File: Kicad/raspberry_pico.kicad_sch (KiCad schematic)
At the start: 5 parts, among them Q1201 DMG2305UX, U1201 Pico

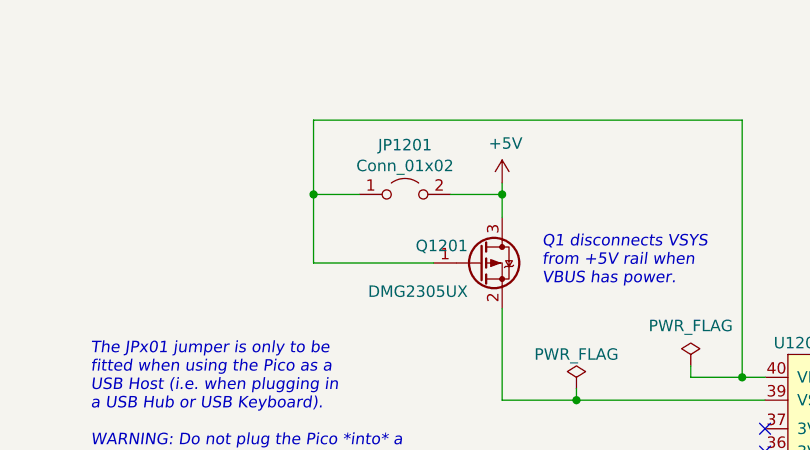
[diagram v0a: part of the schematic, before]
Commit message: Cleaned up the part numbers.
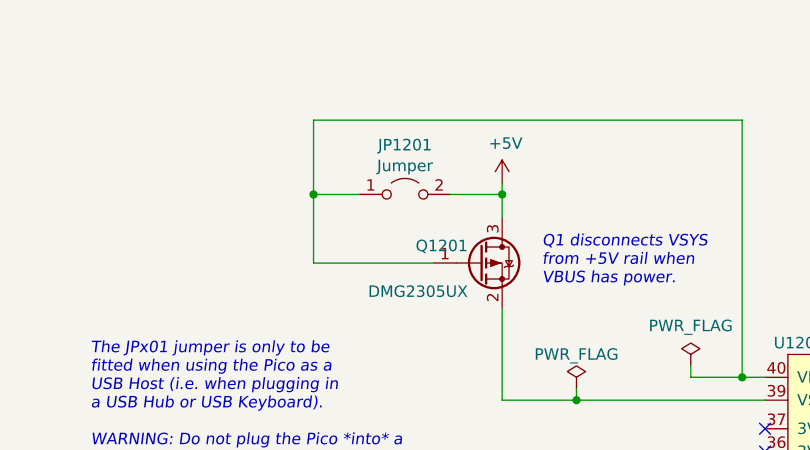
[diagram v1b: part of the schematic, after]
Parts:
- JP1201: value Conn_01x02 -> Jumper
- Q1201: Digikey DMG2305UX-13DICT-ND -> (none); JLCPCB Collection (none) -> Extended
- R1201, R1202: Digikey RMCF0805FT2K00CT-ND -> (none); JLCPCB Collection (none) -> Basic; MPN RMCF0805FT2K00 -> 0805W8F2001T5E; Manufacturer Stackpole -> Uniroyal
- U1201: MPN SC0915 -> Pico
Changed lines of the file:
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@@
       (effects (font (size 1.27 1.27)) hide)
     )
-    (property "MPN" "SC0915" (id 6) (at 132.08 50.8 0)
+    (property "MPN" "Pico" (id 6) (at 132.08 50.8 0)
       (effects (font (size 1.27 1.27)) hide)
     )
@@
     )
     (property "Voltage" "~" (id 11) (at 132.08 50.8 0)
+      (effects (font (size 1.27 1.27)) hide)
+    )
+    (property "JLCPCB Collection" "~" (id 12) (at 132.08 50.8 0)
       (effects (font (size 1.27 1.27)) hide)
     )
@@
       (effects (font (size 1.27 1.27)) hide)
     )
-    (property "Digikey" "RMCF0805FT2K00CT-ND" (id 5) (at 212.725 84.455 0)
-      (effects (font (size 1.27 1.27)) hide)
-    )
-    (property "MPN" "RMCF0805FT2K00" (id 6) (at 212.725 84.455 0)
-      (effects (font (size 1.27 1.27)) hide)
-    )
-    (property "Manufacturer" "Stackpole" (id 7) (at 212.725 84.455 0)
+    (property "Digikey" "~" (id 5) (at 212.725 84.455 0)
+      (effects (font (size 1.27 1.27)) hide)
+    )
+    (property "MPN" "0805W8F2001T5E" (id 6) (at 212.725 84.455 0)
+      (effects (font (size 1.27 1.27)) hide)
+    )
+    (property "Manufacturer" "Uniroyal" (id 7) (at 212.725 84.455 0)
       (effects (font (size 1.27 1.27)) hide)
     )
@@
     )
     (property "Mouser" "~" (id 11) (at 212.725 84.455 0)
+      (effects (font (size 1.27 1.27)) hide)
+    )
+    (property "JLCPCB Collection" "Basic" (id 12) (at 212.725 84.455 0)
       (effects (font (size 1.27 1.27)) hide)
     )
@@
       (effects (font (size 1.27 1.27)) hide)
     )
-    (property "Digikey" "RMCF0805FT2K00CT-ND" (id 5) (at 202.565 84.455 0)
-      (effects (font (size 1.27 1.27)) hide)
-    )
-    (property "MPN" "RMCF0805FT2K00" (id 6) (at 202.565 84.455 0)
-      (effects (font (size 1.27 1.27)) hide)
-    )
-    (property "Manufacturer" "Stackpole" (id 7) (at 202.565 84.455 0)
+    (property "Digikey" "~" (id 5) (at 202.565 84.455 0)
+      (effects (font (size 1.27 1.27)) hide)
+    )
+    (property "MPN" "0805W8F2001T5E" (id 6) (at 202.565 84.455 0)
+      (effects (font (size 1.27 1.27)) hide)
+    )
+    (property "Manufacturer" "Uniroyal" (id 7) (at 202.565 84.455 0)
       (effects (font (size 1.27 1.27)) hide)
     )
@@
       (effects (font (size 1.27 1.27)) hide)
     )
+    (property "JLCPCB Collection" "Basic" (id 12) (at 202.565 84.455 0)
+      (effects (font (size 1.27 1.27)) hide)
+    )
     (pin "1")
     (pin "2")
@@
     (in_bom yes) (on_board yes)
     (property "Reference" "JP1201" (id 0) (at 89.535 27.5336 0))
-    (property "Value" "Conn_01x02" (id 1) (at 89.535 29.845 0))
+    (property "Value" "Jumper" (id 1) (at 89.535 29.845 0))
     (property "Footprint" "Connector_PinHeader_2.54mm:PinHeader_1x02_P2.54mm_Vertical" (id 2) (at 89.535 33.02 0)
       (effects (font (size 1.27 1.27)) hide)
@@
       (effects (font (size 1.27 1.27)) hide)
     )
+    (property "JLCPCB Collection" "~" (id 12) (at 89.535 33.02 0)
+      (effects (font (size 1.27 1.27)) hide)
+    )
     (pin "1")
     (pin "2")
@@
       (effects (font (size 1.27 1.27)) hide)
     )
-    (property "Datasheet" "https://www.diodes.com/assets/Datasheets/DMG2305UX.pdf" (id 3) (at 97.79 40.64 0)
+    (property "Datasheet" "" (id 3) (at 97.79 40.64 0)
       (effects (font (size 1.27 1.27)) hide)
     )
@@
       (effects (font (size 1.27 1.27)) hide)
     )
-    (property "Digikey" "DMG2305UX-13DICT-ND" (id 5) (at 97.79 40.64 0)
+    (property "Digikey" "~" (id 5) (at 97.79 40.64 0)
       (effects (font (size 1.27 1.27)) hide)
     )
@@
       (effects (font (size 1.27 1.27)) hide)
     )
+    (property "JLCPCB Collection" "Extended" (id 12) (at 97.79 40.64 0)
+      (effects (font (size 1.27 1.27)) hide)
+    )

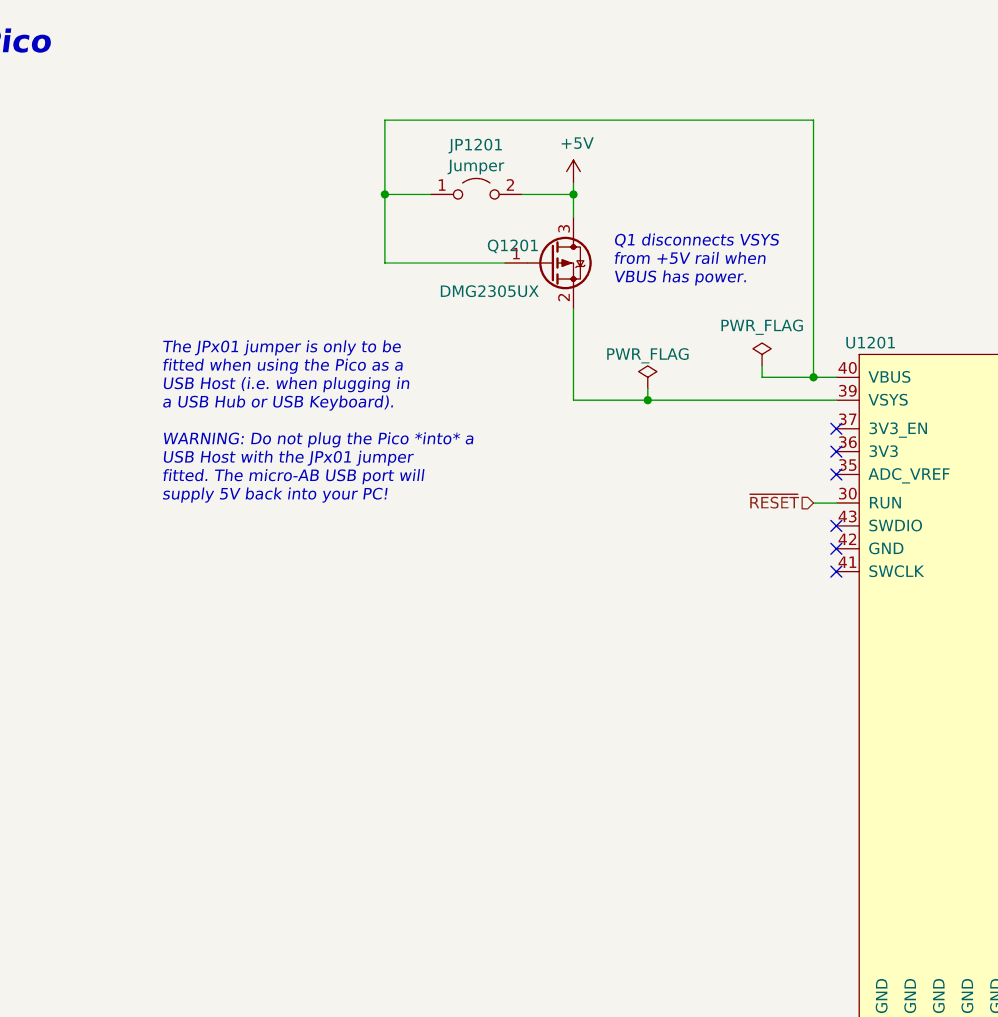
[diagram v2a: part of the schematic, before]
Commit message: Replaced decoupling caps, and worked on PCB layout.
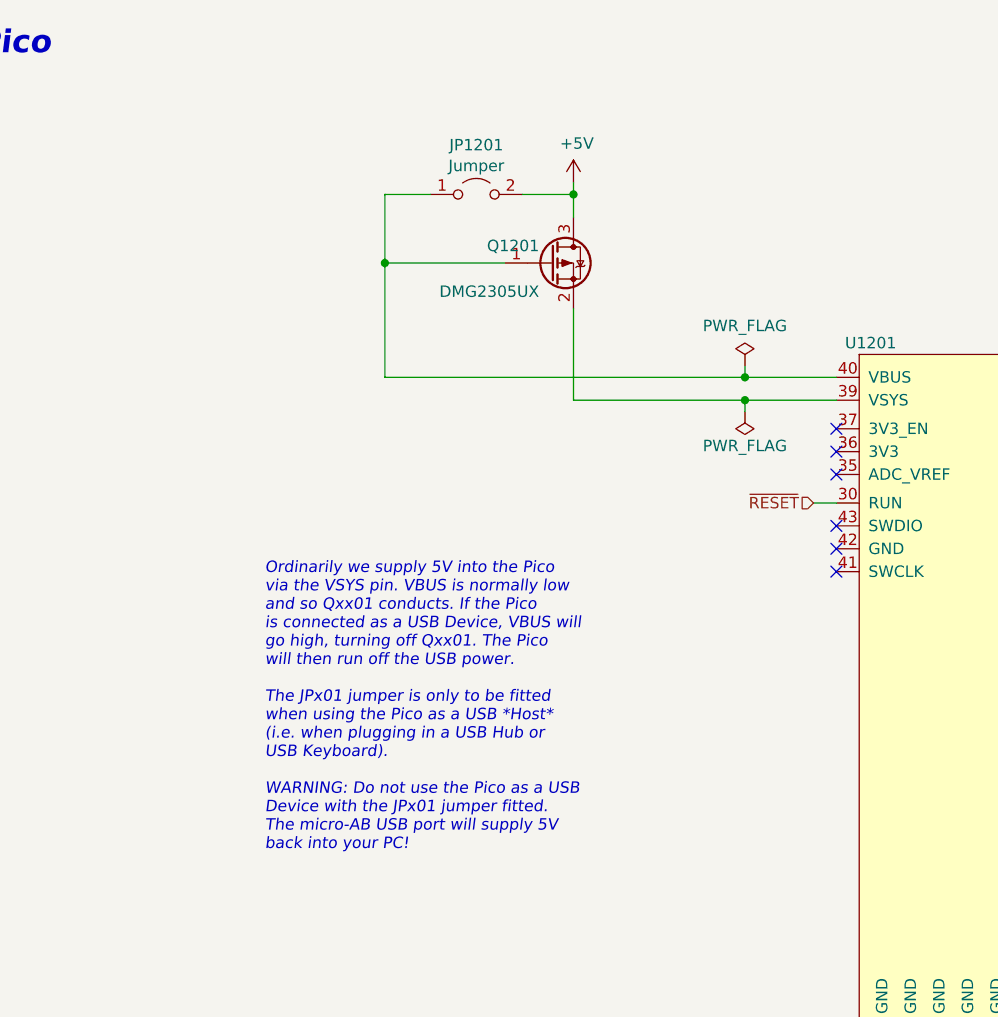
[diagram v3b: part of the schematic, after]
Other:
- note added: "Ordinarily we supply 5V into the Pico via the VSYS pin. VBUS is normally low and so Qxx01 conducts. If the Pico is connected as a USB Device, VBUS will go high, turning off Qxx01. The Pico will then run off the USB power. The JPx01 jumper is only to be fitted when using the Pico as a USB *Host* (i.e. when plugging in a USB Hub or USB Keyboard). WARNING: Do not use the Pico as a USB Device with th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"
- note removed: "Q1 disconnects VSYS from +5V rail when VBUS has power."
- note removed: "The JPx01 jumper is only to be fitted when using the Pico as a USB Host (i.e. when plugging in a USB Hub or USB Keyboard). WARNING: Do not plug the Pico *into* a USB Host with the JPx01 jumper fitted. The micro-AB USB port will supply 5V back into your PC!"
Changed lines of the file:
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@@
     (comment 2 "Copyright (c) The Neotron Developers, 2022")
   )
-  (junction (at 79.375 33.02) (diameter 0) (color 0 0 0 0)
-  )
   (junction (at 150.495 128.27) (diameter 0) (color 0 0 0 0)
   )
   (junction (at 137.795 128.27) (diameter 0) (color 0 0 0 0)
   )
-  (junction (at 108.585 55.88) (diameter 0) (color 0 0 0 0)
+  (junction (at 119.38 55.88) (diameter 0) (color 0 0 0 0)
+  )
+  (junction (at 119.38 53.34) (diameter 0) (color 0 0 0 0)
   )
   (junction (at 144.145 128.27) (diameter 0) (color 0 0 0 0)
@@
   (junction (at 140.97 128.27) (diameter 0) (color 0 0 0 0)
   )
+  (junction (at 79.375 40.64) (diameter 0) (color 0 0 0 0)
+  )
   (junction (at 212.725 79.375) (diameter 0) (color 0 0 0 0)
-  )
-  (junction (at 127 53.34) (diameter 0) (color 0 0 0 0)
   )
   (no_connect (at 129.54 72.39))
@@
     (stroke (width 0) (type default) (color 0 0 0 0))
   )
-  (wire (pts (xy 79.375 24.765) (xy 127 24.765))
+  (wire (pts (xy 79.375 53.34) (xy 119.38 53.34))
     (stroke (width 0) (type default) (color 0 0 0 0))
   )
@@
     (stroke (width 0) (type default) (color 0 0 0 0))
   )
-  (wire (pts (xy 127 24.765) (xy 127 53.34))
-    (stroke (width 0) (type default) (color 0 0 0 0))
-  )
   (wire (pts (xy 165.1 53.34) (xy 167.64 53.34))
     (stroke (width 0) (type default) (color 0 0 0 0))
   )
-  (wire (pts (xy 108.585 54.61) (xy 108.585 55.88))
+  (wire (pts (xy 119.38 57.15) (xy 119.38 55.88))
     (stroke (width 0) (type default) (color 0 0 0 0))
   )
@@
     (stroke (width 0) (type default) (color 0 0 0 0))
   )
+  (wire (pts (xy 119.38 53.34) (xy 129.54 53.34))
+    (stroke (width 0) (type default) (color 0 0 0 0))
+  )
   (wire (pts (xy 212.725 91.44) (xy 212.725 88.265))
     (stroke (width 0) (type default) (color 0 0 0 0))
@@
     (stroke (width 0) (type default) (color 0 0 0 0))
   )
-  (wire (pts (xy 121.285 53.34) (xy 127 53.34))
-    (stroke (width 0) (type default) (color 0 0 0 0))
-  )
   (wire (pts (xy 137.795 128.27) (xy 137.795 127.635))
     (stroke (width 0) (type default) (color 0 0 0 0))
@@
     (stroke (width 0) (type default) (color 0 0 0 0))
   )
-  (wire (pts (xy 127 53.34) (xy 129.54 53.34))
-    (stroke (width 0) (type default) (color 0 0 0 0))
-  )
   (wire (pts (xy 94.615 33.02) (xy 100.33 33.02))
     (stroke (width 0) (type default) (color 0 0 0 0))
@@
     (stroke (width 0) (type default) (color 0 0 0 0))
   )
-  (wire (pts (xy 108.585 55.88) (xy 129.54 55.88))
+  (wire (pts (xy 119.38 55.88) (xy 129.54 55.88))
     (stroke (width 0) (type default) (color 0 0 0 0))
   )
@@
     (stroke (width 0) (type default) (color 0 0 0 0))
   )
-  (wire (pts (xy 100.33 55.88) (xy 108.585 55.88))
+  (wire (pts (xy 100.33 55.88) (xy 119.38 55.88))
     (stroke (width 0) (type default) (color 0 0 0 0))
   )
@@
     (stroke (width 0) (type default) (color 0 0 0 0))
   )
-  (wire (pts (xy 79.375 24.765) (xy 79.375 33.02))
+  (wire (pts (xy 79.375 53.34) (xy 79.375 40.64))
     (stroke (width 0) (type default) (color 0 0 0 0))
   )
@@
     (stroke (width 0) (type default) (color 0 0 0 0))
   )
-  (wire (pts (xy 121.285 52.07) (xy 121.285 53.34))
+  (wire (pts (xy 119.38 52.07) (xy 119.38 53.34))
     (stroke (width 0) (type default) (color 0 0 0 0))
   )
@@
     (stroke (width 0) (type default) (color 0 0 0 0))
   )
-  (text "Q1 disconnects VSYS\nfrom +5V rail when\nVBUS has power."
-    (at 104.775 43.18 0)
-    (effects (font (size 1.27 1.27) italic) (justify left bottom))
-  )
-  (text "The JPx01 jumper is only to be\nfitted when using the Pico as a\nUSB Host (i.e. when plugging in\na USB Hub or USB Keyboard).\n\nWARNING: Do not plug the Pico *into* a\nUSB Host with the JPx01 jumper\nfitted. The micro-AB USB port will\nsupply 5V back into your PC!"
-    (at 54.61 67.31 0)
+  (text "Ordinarily we supply 5V into the Pico\nvia the VSYS pin. VBUS is normally low\nand so Qxx01 conducts. If the Pico\nis connected as a USB Device, VBUS will\ngo high, turning off Qxx01. The Pico\nwill then run off the USB power.\n\nThe JPx01 jumper is only to be fitted\nwhen using the Pico as a USB *Host*\n(i.e. when plugging in a USB Hub or\nUSB Keyboard).\n\nWARNING: Do not use the Pico as a USB\nDevice with the JPx01 jumper fitted.\nThe micro-AB USB port will supply 5V\nback into your PC!"
+    (at 66.04 106.045 0)
     (effects (font (size 1.27 1.27) italic) (justify left bottom))
   )
@@
     (pin "9")
   )
-  (symbol (lib_id "power:PWR_FLAG") (at 121.285 52.07 0) (mirror y) (unit 1)
-    (in_bom yes) (on_board yes)
-    (property "Reference" "#FLG01201" (id 0) (at 121.285 50.165 0)
-      (effects (font (size 1.27 1.27)) hide)
-    )
-    (property "Value" "PWR_FLAG" (id 1) (at 121.285 47.625 0))
-    (property "Footprint" "" (id 2) (at 121.285 52.07 0)
-      (effects (font (size 1.27 1.27)) hide)
-    )
-    (property "Datasheet" "~" (id 3) (at 121.285 52.07 0)
+  (symbol (lib_id "power:PWR_FLAG") (at 119.38 52.07 0) (mirror y) (unit 1)
+    (in_bom yes) (on_board yes)
+    (property "Reference" "#FLG01201" (id 0) (at 119.38 50.165 0)
+      (effects (font (size 1.27 1.27)) hide)
+    )
+    (property "Value" "PWR_FLAG" (id 1) (at 119.38 47.625 0))
+    (property "Footprint" "" (id 2) (at 119.38 52.07 0)
+      (effects (font (size 1.27 1.27)) hide)
+    )
+    (property "Datasheet" "~" (id 3) (at 119.38 52.07 0)
       (effects (font (size 1.27 1.27)) hide)
     )
@@
     (pin "1")
   )
-  (symbol (lib_id "power:PWR_FLAG") (at 108.585 54.61 0) (mirror y) (unit 1)
-    (in_bom yes) (on_board yes)
-    (property "Reference" "#FLG01202" (id 0) (at 108.585 52.705 0)
-      (effects (font (size 1.27 1.27)) hide)
-    )
-    (property "Value" "PWR_FLAG" (id 1) (at 108.585 50.8 0))
-    (property "Footprint" "" (id 2) (at 108.585 54.61 0)
-      (effects (font (size 1.27 1.27)) hide)
-    )
-    (property "Datasheet" "~" (id 3) (at 108.585 54.61 0)
+  (symbol (lib_id "power:PWR_FLAG") (at 119.38 57.15 0) (mirror x) (unit 1)
+    (in_bom yes) (on_board yes)
+    (property "Reference" "#FLG01202" (id 0) (at 119.38 59.055 0)
+      (effects (font (size 1.27 1.27)) hide)
+    )
+    (property "Value" "PWR_FLAG" (id 1) (at 119.38 60.96 0))
+    (property "Footprint" "" (id 2) (at 119.38 57.15 0)
+      (effects (font (size 1.27 1.27)) hide)
+    )
+    (property "Datasheet" "~" (id 3) (at 119.38 57.15 0)
       (effects (font (size 1.27 1.27)) hide)
     )
@@
       (effects (font (size 1.27 1.27)) hide)
     )
-    (property "Datasheet" "" (id 3) (at 97.79 40.64 0)
-      (effects (font (size 1.27 1.27)) hide)
-    )
+    (property "Datasheet" "https://datasheet.lcsc.com/lcsc/1809061415_Diodes-Incorporated-DMG2305UX-13_C144153.pdf" (id 3) (at 97.79 40.64 0)
+      (effects (font (size 1.27 1.27)) hide)
+    )

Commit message: Added source resistors on SPI bus.
Also renumbered pages.
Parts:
- added C201, C202: DNF, Capacitor_SMD:C_0805_2012Metric_Pad1.18x1.45mm_HandSolder, symbol Device:C
- added R203, R204: 0R, Resistor_SMD:R_0805_2012Metric_Pad1.20x1.40mm_HandSolder, symbol Device:R
- renumbered JP1201 to JP201, Q1201 to Q201, R1201 to R201, R1202 to R202, U1201 to U201
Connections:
- net GND: now also C201.2, C202.2
- net SPI_CLK: now also C201.1, R203.2; no longer U201.24 (GPIO18)
- net SPI_COPI: now also C202.1, R204.2; no longer U201.25 (GPIO19)
- new net: R203.1, U201.24 (GPIO18)
- new net: R204.1, U201.25 (GPIO19)
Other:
- note added: "These signals drive a multiple nodes on the bus, so we have the option of fitting resistors here at the source to reduce slew rate and try to dampen ringing."

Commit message: Make USB power jump DNP=0
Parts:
- JP201: DNP 1 -> 0
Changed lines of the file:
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@@
       (effects (font (size 1.27 1.27)) hide)
     )
-    (property "DNP" "1" (id 4) (at 89.535 33.02 0)
+    (property "DNP" "0" (id 4) (at 89.535 33.02 0)
       (effects (font (size 1.27 1.27)) hide)
     )

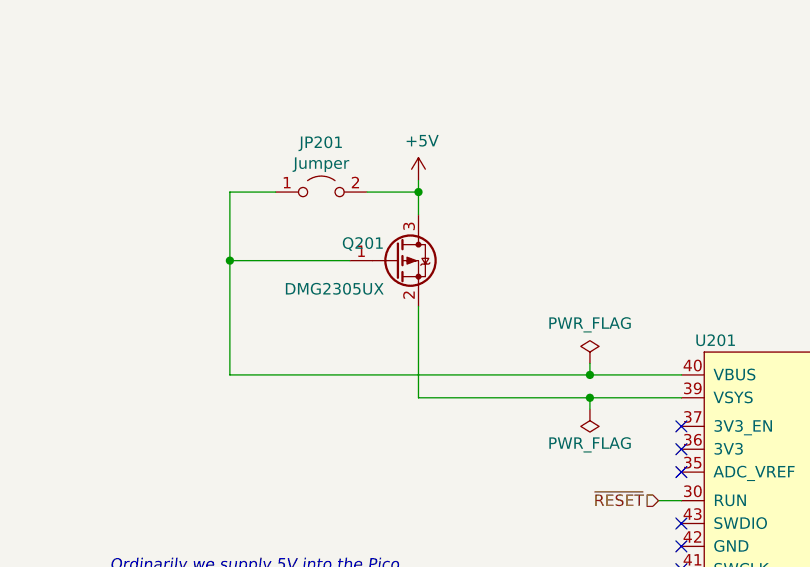
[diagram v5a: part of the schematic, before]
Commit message: Updated to KiCAD 7.
Had to move a net-tie to resolve a "too close" error.
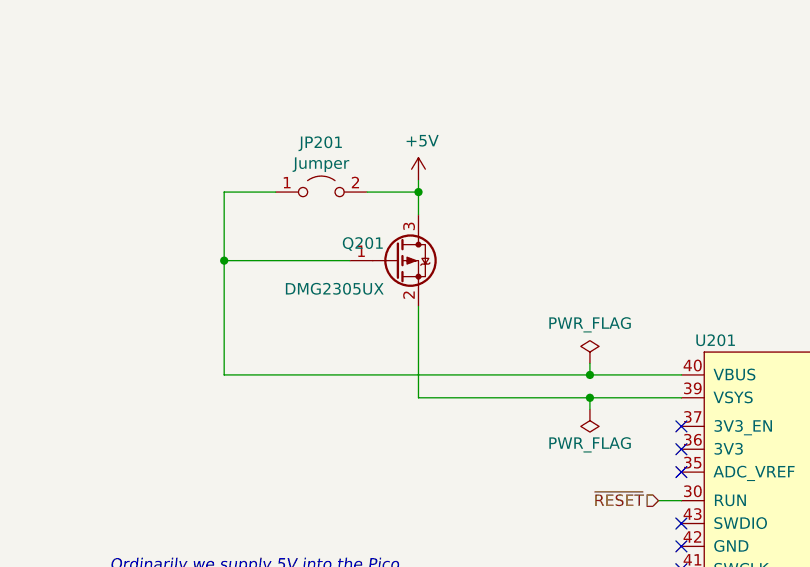
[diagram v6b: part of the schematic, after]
